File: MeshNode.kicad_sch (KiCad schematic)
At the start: 31 parts, among them J1 MicroSD_Module, J2 AHT20+BMP280, J3 Solar, J4 Battery, J5 I2C pins, Q1 IRLZ44N, U3 MIC5219-3.3YM5

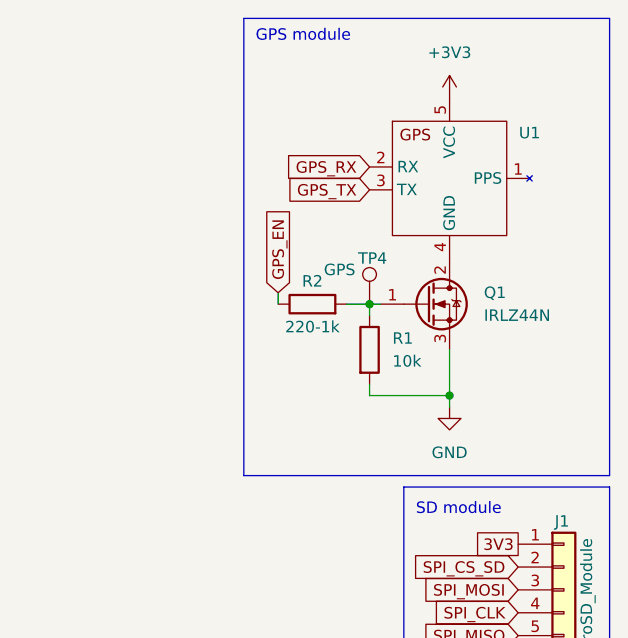
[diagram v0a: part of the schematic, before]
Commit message: Changed FET, resized traces, connected S22 connections
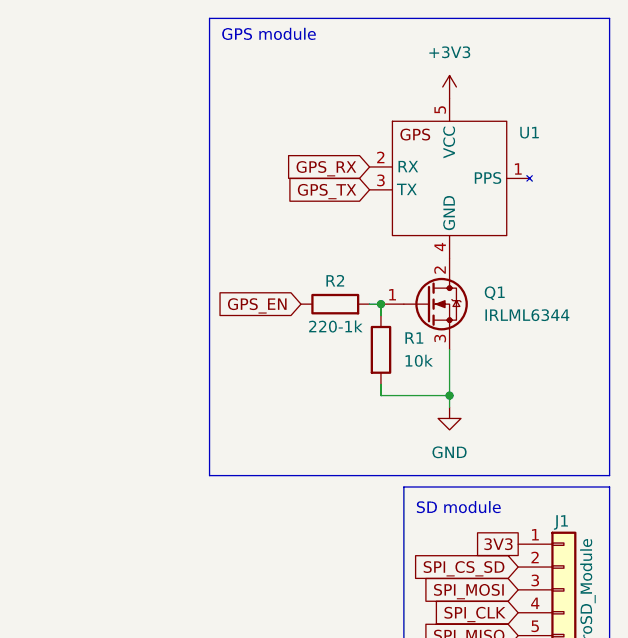
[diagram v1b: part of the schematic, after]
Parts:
- removed TP4: GPS, TestPoint:TestPoint_Plated_Hole_D2.0mm, symbol Connector:TestPoint
- Q1: value IRLZ44N -> IRLML6344; footprint Package_TO_SOT_THT:TO-220-3_Vertical -> Package_TO_SOT_SMD:SOT-23
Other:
- moved on the sheet: R1, R2
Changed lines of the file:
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@@
 	)
 	(junction
-		(at 256.54 44.45)
-		(diameter 0)
-		(color 0 0 0 0)
-	)
-	(junction
 		(at 29.21 25.4)
 		(diameter 0)
@@
 	)
 	(junction
+		(at 257.81 44.45)
+		(diameter 0)
+		(color 0 0 0 0)
+	)
+	(junction
 		(at 163.83 87.63)
 		(diameter 0)
@@
 	(wire
 		(pts
+			(xy 256.54 44.45) (xy 257.81 44.45)
+		)
+		(stroke
+			(width 0)
+			(type default)
+		)
+	)
+	(wire
+		(pts
 			(xy 54.61 25.4) (xy 58.42 25.4)
 		)
@@
 	(wire
 		(pts
-			(xy 256.54 54.61) (xy 265.43 54.61)
+			(xy 257.81 54.61) (xy 265.43 54.61)
 		)
 		(stroke
@@
 	(wire
 		(pts
-			(xy 256.54 45.72) (xy 256.54 44.45)
+			(xy 257.81 45.72) (xy 257.81 44.45)
 		)
 		(stroke
@@
 	(wire
 		(pts
-			(xy 256.54 53.34) (xy 256.54 54.61)
+			(xy 257.81 53.34) (xy 257.81 54.61)
 		)
 		(stroke
@@
 	(wire
 		(pts
-			(xy 256.54 44.45) (xy 257.81 44.45)
-		)
-		(stroke
-			(width 0)
-			(type default)
-		)
-	)
-	(wire
-		(pts
 			(xy 162.56 87.63) (xy 163.83 87.63)
 		)
@@
 	(wire
 		(pts
-			(xy 254 44.45) (xy 256.54 44.45)
-		)
-		(stroke
-			(width 0)
-			(type default)
-		)
-	)
-	(wire
-		(pts
 			(xy 80.01 27.94) (xy 78.74 27.94)
 		)
@@
 	(wire
 		(pts
-			(xy 246.38 43.18) (xy 246.38 44.45)
-		)
-		(stroke
-			(width 0)
-			(type default)
-		)
-	)
-	(wire
-		(pts
 			(xy 184.15 85.09) (xy 184.15 87.63)
 		)
@@
 	)
 	(rectangle
-		(start 242.57 12.7)
+		(start 238.76 12.7)
 		(end 283.21 63.5)
 		(stroke
@@
 	(text "GPS module"
 		(exclude_from_sim no)
-		(at 249.174 14.732 0)
+		(at 245.364 14.732 0)
 		(effects
 			(font
@@
 	(global_label "GPS_EN"
 		(shape input)
-		(at 246.38 43.18 90)
+		(at 248.92 44.45 180)
 		(fields_autoplaced yes)
 		(effects
@@
 				(size 1.27 1.27)
 			)
-			(justify left)
+			(justify right)
 		)
 		(property "Intersheetrefs" "${INTERSHEET_REFS}"
-			(at 246.38 32.9982 90)
+			(at 238.7382 44.45 0)
 			(effects
 				(font
 					(size 1.27 1.27)
 				)
-				(justify left)
+				(justify right)
 				(hide yes)
 			)
@@
 	(symbol
 		(lib_id "Device:R")
-		(at 256.54 49.53 0)
+		(at 257.81 49.53 0)
 		(unit 1)
 		(exclude_from_sim no)
@@
 		(fields_autoplaced yes)
 		(property "Reference" "R1"
-			(at 259.08 48.2599 0)
+			(at 260.35 48.2599 0)
 			(effects
 				(font
@@
 		)
 		(property "Value" "10k"
-			(at 259.08 50.7999 0)
+			(at 260.35 50.7999 0)
 			(effects
 				(font
@@
 		)
 		(property "Footprint" "Resistor_SMD:R_0603_1608Metric"
-			(at 254.762 49.53 90)
+			(at 256.032 49.53 90)
 			(effects
 				(font
@@
 		)
 		(property "Datasheet" "~"
-			(at 256.54 49.53 0)
+			(at 257.81 49.53 0)
 			(effects
 				(font
@@
 		)
 		(property "Description" "Resistor"
-			(at 256.54 49.53 0)
+			(at 257.81 49.53 0)
 			(effects
 				(font
@@
 	(symbol
 		(lib_id "Device:R")
-		(at 250.19 44.45 90)
+		(at 252.73 44.45 90)
 		(unit 1)
 		(exclude_from_sim no)
@@
 		(dnp no)
 		(property "Reference" "R2"
-			(at 250.19 41.91 90)
+			(at 252.73 41.91 90)
 			(effects
 				(font
@@
 		)
 		(property "Value" "220-1k"
-			(at 250.19 46.99 90)
+			(at 252.73 46.99 90)
 			(effects
 				(font
@@
 		)
 		(property "Footprint" "Resistor_SMD:R_0603_1608Metric"
-			(at 250.19 46.228 90)
+			(at 252.73 46.228 90)
 			(effects
 				(font
@@
 		)
 		(property "Datasheet" "~"
-			(at 250.19 44.45 0)
+			(at 252.73 44.45 0)
 			(effects
 				(font
@@
 		)
 		(property "Description" "Resistor"
-			(at 250.19 44.45 0)
+			(at 252.73 44.45 0)
 			(effects
 				(font
@@
 	)
 	(symbol
-		(lib_id "Connector:TestPoint")
-		(at 256.54 44.45 0)
-		(unit 1)
-		(exclude_from_sim no)
-		(in_bom yes)
-		(on_board yes)
-		(dnp no)
-		(property "Reference" "TP4"
-			(at 255.27 39.37 0)
-			(effects
-				(font
-					(size 1.27 1.27)
-				)
-				(justify left)
-			)
-		)
-		(property "Value" "GPS"
-			(at 251.46 40.64 0)
-			(effects
-				(font
-					(size 1.27 1.27)
-				)
-				(justify left)
-			)
-		)
-		(property "Footprint" "TestPoint:TestPoint_Plated_Hole_D2.0mm"
-			(at 261.62 44.45 0)
-			(effects
-				(font
-					(size 1.27 1.27)
-				)
-				(hide yes)
-			)
-		)
-		(property "Datasheet" "~"
-			(at 261.62 44.45 0)
-			(effects
-				(font
-					(size 1.27 1.27)
-				)
-				(hide yes)
-			)
-		)
-		(property "Description" "test point"
-			(at 256.54 44.45 0)
-			(effects
-				(font
-					(size 1.27 1.27)
-				)
-				(hide yes)
-			)
-		)
-		(pin "1"
-		)
-		(instances
-			(project "MeshNode"
-				(path "/cb11cd72-88ca-4db8-ba82-5b84ed918fd9"
-					(reference "TP4")
-					(unit 1)
-				)
-			)
-		)
-	)
-	(symbol
 		(lib_id "Mechanical:MountingHole")
 		(at 17.78 177.8 0)
@@
 			)
 		)
-		(property "Value" "IRLZ44N"
+		(property "Value" "IRLML6344"
 			(at 269.24 45.7199 0)
 			(effects
@@
 			)
 		)
-		(property "Footprint" "Package_TO_SOT_THT:TO-220-3_Vertical"
+		(property "Footprint" "Package_TO_SOT_SMD:SOT-23"
 			(at 267.97 46.355 0)
 			(effects
